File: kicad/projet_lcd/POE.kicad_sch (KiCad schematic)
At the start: 79 parts, among them Q1 FOD817A3SD

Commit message: cleanup
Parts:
- U3: footprint Voltage_Regulators:TL431 -> Voltage_regulators:TL431
- U4: footprint Voltage_Regulators:AMS1117-3.3 -> Voltage_regulators:AMS1117-3.3
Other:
- moved on the sheet: C55, C56, TP13, U4

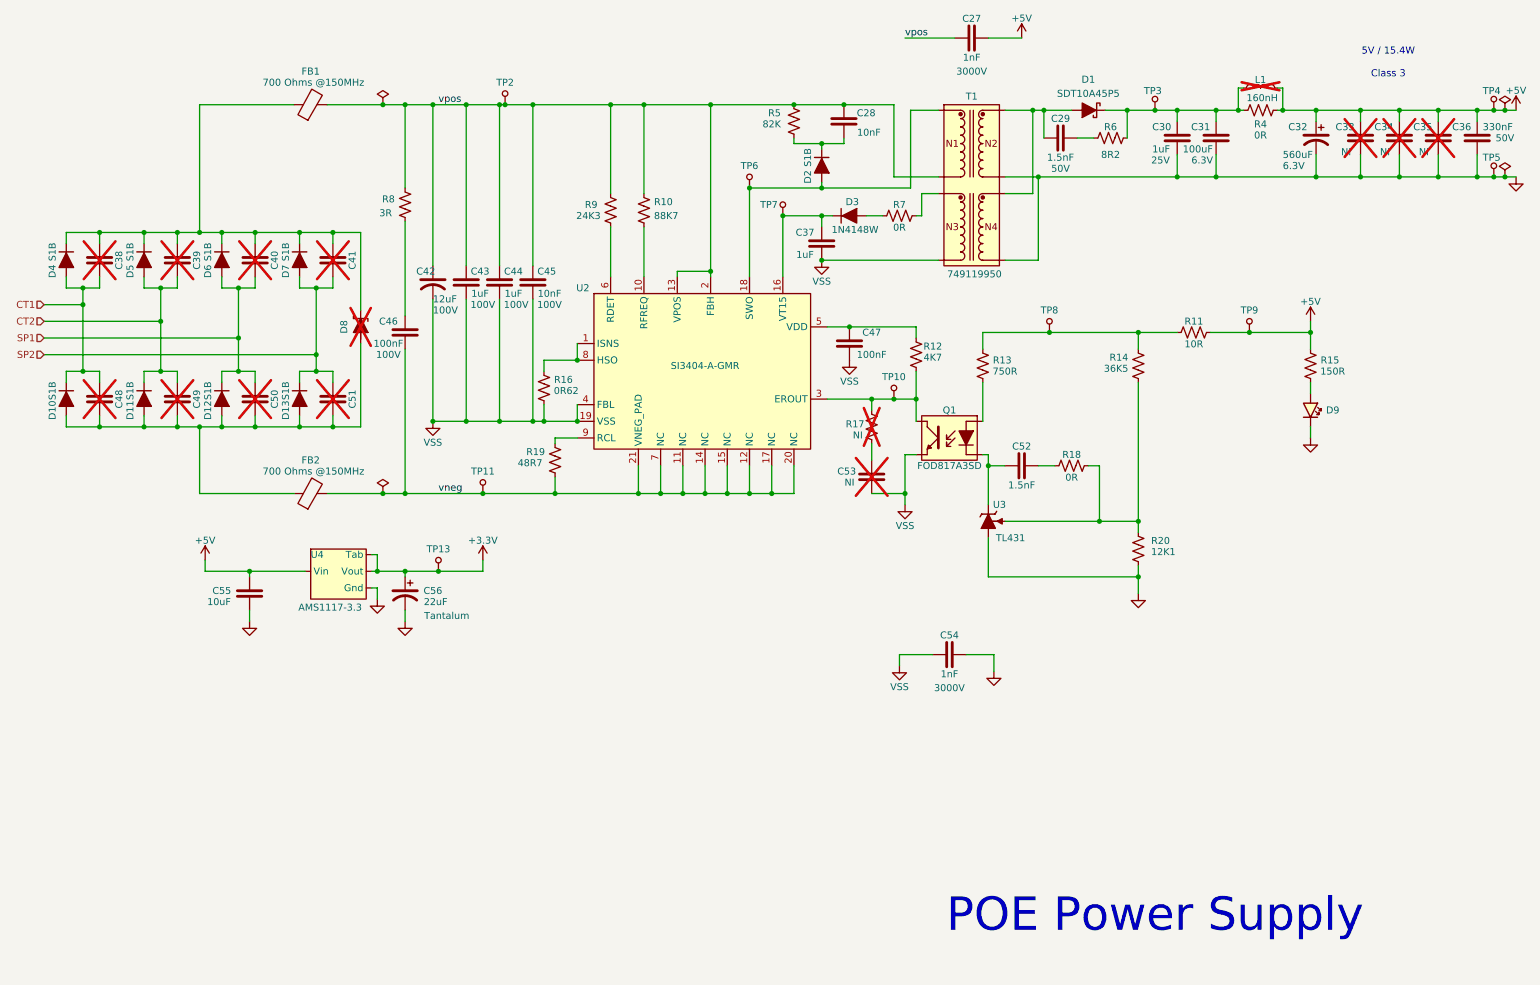
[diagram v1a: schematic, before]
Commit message: cleaning up ERC alerts
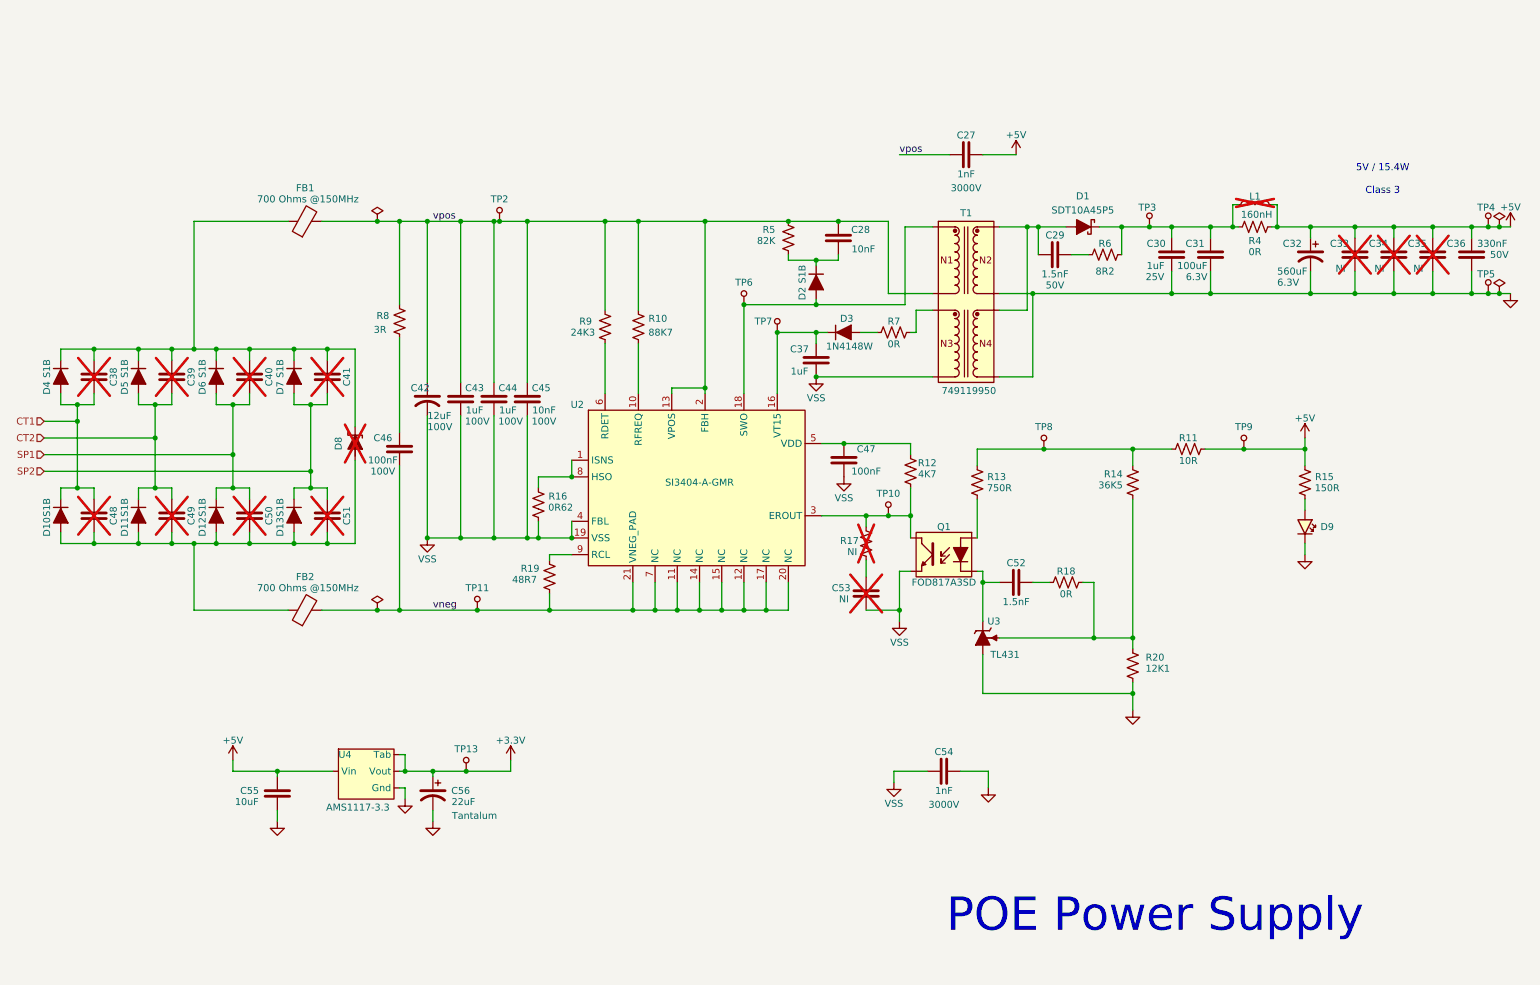
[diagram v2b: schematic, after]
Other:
- moved on the sheet: C27, C28, C29, C30, C31, C32, C33, C34, C35, C36, C37, C38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

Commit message: on avance !
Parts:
- added C84: 10uF, Generics:C_0603, symbol Generics:C
- added C85: 22uF, Generics:C_tantalum_A, symbol Generics:C_Polarized
- added TP12: ~, PCB_Utils:TP_1.5, symbol PCB_Utils:TP
- added U9: ~, Voltage_regulators:AMS1117-3.3, symbol Voltage_Regulators:AMS1117-3.3
- C42: footprint (none) -> Generics:C_ALU_G13
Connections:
- net +5V: now also C84.2, U9.3 (Vin)
- net GND: now also C84.1, C85.N, U9.Gnd
- new net Vaux_3V3: C85.P, TP12.1, U9.2 (Vout), U9.4 (Tab)

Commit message: routage en cours
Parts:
- removed C42: 12uF, Generics:C_ALU_G13, symbol Generics:C_alt
- added C86: 12uF, Passives:C487495, symbol Passives:C_12uF_200V
- D1, D9: Part# (none) -> NI
- D10, D11, D12, D13, D2, D4, D5, D6, D7: Part# S1B -> NI
- D3: Part# 1N4148W -> NI
- D8: Part# SMAJ58A -> NI
- U3: footprint Voltage_regulators:TL431 -> Voltage_Regulators:TL431
- U4, U9: footprint Voltage_regulators:AMS1117-3.3 -> Voltage_Regulators:AMS1117-3.3
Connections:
- net VSS: now also C86.N
- net vpos: now also C86.P
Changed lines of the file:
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@@
 			)
 		)
-		(property "Part#" "S1B"
+		(property "Part#" "NI"
 			(at 46.5 102.5 0)
 			(do_not_autoplace yes)
@@
 			)
 		)
-		(property "Part#" "1N4148W"
+		(property "Part#" "NI"
 			(at 163 73.5 0)
 			(do_not_autoplace yes)
@@
 	)
 	(symbol
-		(lib_id "Generics:C_alt")
-		(at 87 86 90)
-		(unit 1)
-		(exclude_from_sim no)
-		(in_bom yes)
-		(on_board yes)
-		(dnp no)
-		(property "Reference" "C42"
-			(at 84 81 90)
-			(effects
-				(font
-					(size 1.27 1.27)
-				)
-				(justify right)
-			)
-		)
-		(property "Value" "12uF"
-			(at 87 86 90)
-			(effects
-				(font
-					(size 1.27 1.27)
-				)
-				(justify right)
-			)
-		)
-		(property "Footprint" "Generics:C_ALU_G13"
-			(at 90.0652 84.11 90)
-			(effects
-				(font
-					(size 1.25 1.25)
-				)
-				(hide yes)
-			)
-		)
-		(property "Datasheet" ""
-			(at 102 86 90)
-			(effects
-				(font
-					(size 1.25 1.25)
-				)
-				(hide yes)
-			)
-		)
-		(property "Description" "Unpolarized capacitor (alt)"
-			(at 92.5 82.9 0)
-			(effects
-				(font
-					(size 1.25 1.25)
-				)
-				(hide yes)
-			)
-		)
-		(property "Manufacturer" "Panasonic"
-			(at 100 83 0)
-			(effects
-				(font
-					(size 1.27 1.27)
-				)
-				(hide yes)
-			)
-		)
-		(property "Part#" "EEUFC2A120"
-			(at 87 86 0)
-			(effects
-				(font
-					(size 1.25 1.25)
-				)
-				(hide yes)
-			)
-		)
-		(property "LCSC Part#" ""
-			(at 87 86 0)
-			(effects
-				(font
-					(size 1.27 1.27)
-				)
-				(hide yes)
-			)
-		)
-		(property "Voltage" "100V"
-			(at 87 88 90)
-			(effects
-				(font
-					(size 1.27 1.27)
-				)
-				(justify right)
-			)
-		)
-		(property "Comments" ""
-			(at 87 86 0)
-			(effects
-				(font
-					(size 1.25 1.25)
-				)
-				(hide yes)
-			)
-		)
-		(property "LCSC Part #" ""
-			(at 87 86 0)
-			(effects
-				(font
-					(size 1.27 1.27)
-				)
-				(hide yes)
-			)
-		)
-		(pin "1"
-		)
-		(pin "2"
-		)
-		(instances
-			(project ""
-				(path "/b3ce22de-813e-4a84-80c2-bec39c904000/4cd1692b-280a-46ef-a0ce-bb76541e4c5a"
-					(reference "C42")
-					(unit 1)
-				)
-			)
-		)
-	)
-	(symbol
 		(lib_id "Generics:R")
 		(at 245 101 90)
@@
 			)
 		)
-		(property "Part#" "S1B"
+		(property "Part#" "NI"
 			(at 18.5 77.5 0)
 			(do_not_autoplace yes)
@@
 			)
 		)
-		(property "Part#" "S1B"
+		(property "Part#" "NI"
 			(at 60.5 77.5 0)
 			(do_not_autoplace yes)
@@
 			)
 		)
-		(property "Part#" ""
+		(property "Part#" "NI"
 			(at 242.5 106 0)
 			(do_not_autoplace yes)
@@
 			)
 		)
-		(property "Part#" ""
+		(property "Part#" "NI"
 			(at 205.4785 47.67 0)
 			(effects
@@
 			)
 		)
-		(property "Part#" "S1B"
+		(property "Part#" "NI"
 			(at 60.5 102.5 0)
 			(do_not_autoplace yes)
@@
 			)
 		)
-		(property "Part#" "S1B"
+		(property "Part#" "NI"
 			(at 32.5 77.5 0)
 			(do_not_autoplace yes)
@@
 			)
 		)
-		(property "Part#" "S1B"
+		(property "Part#" "NI"
 			(at 18.5 102.5 0)
 			(do_not_autoplace yes)
@@
 			)
 		)
-		(property "Footprint" "Voltage_regulators:AMS1117-3.3"
+		(property "Footprint" "Voltage_Regulators:AMS1117-3.3"
 			(at 70 175 0)
 			(effects
@@
 	)
 	(symbol
+		(lib_id "Passives:C_12uF_200V")
+		(at 87 86 90)
+		(unit 1)
+		(exclude_from_sim no)
+		(in_bom yes)
+		(on_board yes)
+		(dnp no)
+		(property "Reference" "C86"
+			(at 83 81 90)
+			(effects
+				(font
+					(size 1.27 1.27)
+				)
+				(justify right)
+			)
+		)
+		(property "Value" "12uF"
+			(at 88 86 90)
+			(effects
+				(font
+					(size 1.27 1.27)
+				)
+				(justify right)
+			)
+		)
+		(property "Footprint" "Passives:C487495"
+			(at 79 85.9 0)
+			(effects
+				(font
+					(size 1.27 1.27)
+				)
+				(hide yes)
+			)
+		)
+		(property "Datasheet" ""
+			(at 87 86 0)
+			(effects
+				(font
+					(size 1.27 1.27)
+				)
+				(hide yes)
+			)
+		)
+		(property "Description" "12uF 100V 20% Aluminium - Ymin VKMD1252D120MV"
+			(at 80.8 86 0)
+			(effects
+				(font
+					(size 1.27 1.27)
+				)
+				(hide yes)
+			)
+		)
+		(property "LCSC Part#" "C487495"
+			(at 75.4 85.9 0)
+			(effects
+				(font
+					(size 1.27 1.27)
+				)
+				(hide yes)
+			)
+		)
+		(property "Part#" "VKMD1252D120MV"
+			(at 77.1 86 0)
+			(effects
+				(font
+					(size 1.27 1.27)
+				)
+				(hide yes)
+			)
+		)
+		(property "Rated Voltage" "200V"
+			(at 88 88 90)
+			(effects
+				(font
+					(size 1.27 1.27)
+				)
+				(justify right)
+			)
+		)
+		(pin "N"
+		)
+		(pin "P"
+		)
+		(instances
+			(project ""
+				(path "/b3ce22de-813e-4a84-80c2-bec39c904000/4cd1692b-280a-46ef-a0ce-bb76541e4c5a"
+					(reference "C86")
+					(unit 1)
+				)
+			)
+		)
+	)
+	(symbol
 		(lib_id "Generics:C")
 		(at 177 150 0)
@@
 			)
 		)
-		(property "Footprint" "Voltage_regulators:TL431"
+		(property "Footprint" "Voltage_Regulators:TL431"
 			(at 187 123 0)
 			(effects
@@
 			)
 		)
-		(property "Footprint" "Voltage_regulators:AMS1117-3.3"
+		(property "Footprint" "Voltage_Regulators:AMS1117-3.3"
 			(at 70 150 0)
 			(effects
@@
 			)
 		)
-		(property "Part#" "S1B"
+		(property "Part#" "NI"
 			(at 154.5 60.5 0)
 			(do_not_autoplace yes)
@@
 			)
 		)
-		(property "Part#" "S1B"
+		(property "Part#" "NI"
 			(at 46.5 77.5 0)
 			(do_not_autoplace yes)
@@
 			)
 		)
-		(property "Part#" "S1B"
+		(property "Part#" "NI"
 			(at 32.5 102.5 0)
 			(do_not_autoplace yes)
@@
 			)
 		)
-		(property "Part#" "SMAJ58A"
+		(property "Part#" "NI"
 			(at 71 89 0)
 			(do_not_autoplace yes)
